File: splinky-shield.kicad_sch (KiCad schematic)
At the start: 40 parts, among them J1 USB_C_Receptacle_USB2.0, J2 Conn_01x12, J3 Conn_01x05, J4 Conn_01x12, J5 Conn_01x02, SW1 SW_Push, SW2 SW_Push, U1 RP2040, U2 GD25Q80CEIGR, U3 XC6210B332MR-G, Y1 Crystal_GND24

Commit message: routing
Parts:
- removed J2, J4: Conn_01x12, 0xLib_Connectors:PinHeader_1x12_P2.54mm, symbol Connector_Generic:Conn_01x12
- removed J3: Conn_01x05, 0xLib_Connectors:PinHeader_1x05_P2.54mm, symbol Connector_Generic:Conn_01x05
- added J10: Ribbon, Library:5_PinHeader, symbol Connector:Conn_01x05_Female
- added J11, J6: Serial, Library:Jack_3.5mm_PJ320E_Horizontal, symbol Connector:AudioJack4
- added J2, J3: Conn_01x04_Female, Connector_PinSocket_2.54mm:PinSocket_1x04_P2.54mm_Vertical, symbol Connector:Conn_01x04_Female
- added J7: trackball, Library:6_PinHeader, symbol Connector:Conn_01x06_Female
- added J8: Ribbon, Library:6_PinHeader, symbol Connector:Conn_01x06_Female
- added J9: RGB, Library:header1x03, symbol Connector:Conn_01x03_Female
- added JP1, JP2: Jumper_2_Open, local-libraries:SolderJumper-2_P1.3mm_Open_RoundedPad1.0x1.5mm, symbol Jumper:Jumper_2_Open
- added SW3: SW_SPST, Library:PushSwitch, symbol Switch:SW_SPST
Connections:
- net +5V: now also J2.1 (Pin_1), J3.1 (Pin_1), J7.1 (Pin_1), J9.1 (Pin_1), JP1.2 (B), JP2.2 (B)
- net D+: now also J2.4 (Pin_4), J3.4 (Pin_4)
- net D-: now also J2.3 (Pin_3), J3.3 (Pin_3)
- net GND: now also J11.R1, J2.2 (Pin_2), J3.2 (Pin_2), J6.R1, J7.6 (Pin_6), J9.2 (Pin_2), SW3.2 (B)
- net A0 renamed row2_l
- net row2_l: now also J10.5 (Pin_5)
- net A1 renamed col1_l
- net col1_l: now also J10.4 (Pin_4)
- net A2 renamed col2_l
- net col2_l: now also J10.3 (Pin_3)
- net A3 renamed row1_l
- net row1_l: now also J10.2 (Pin_2)
- net D0 renamed rgb_r
- net rgb_r: now also J9.3 (Pin_3)
- net D1 renamed serial_l
- net serial_l: now also J11.R2, J6.R2
- net D12: no longer names the net of U1.15 (GPIO12)
- net D13: no longer names the net of U1.16 (GPIO13)
- net D14: no longer names the net of U1.17 (GPIO14)
- net D15 renamed split_hand_l
- net D16 renamed ss_l
- net ss_l: now also J7.2 (Pin_2)
- net D2: no longer names the net of U1.4 (GPIO2)
- net D21 renamed col3_l
- net col3_l: now also J10.1 (Pin_1)
- net D3: no longer names the net of U1.5 (GPIO3)
- net D4 renamed row4_l
- net row4_l: now also J8.1 (Pin_1)
- net D5 renamed row3_l
- net row3_l: now also J8.2 (Pin_2)
- net D6 renamed col4_l
- net col4_l: now also J8.3 (Pin_3)
- net D7 renamed col5_l
- net col5_l: now also J8.4 (Pin_4)
- net D8 renamed col6_l
- net col6_l: now also J8.5 (Pin_5)
- net D9 renamed row5_l
- net row5_l: now also J8.6 (Pin_6)
- net MISO renamed miso_l
- net miso_l: now also J7.5 (Pin_5)
- net MOSI renamed mosi_l
- net mosi_l: now also J7.3 (Pin_3)
- net SCLK renamed sc_l
- net sc_l: now also J7.4 (Pin_4)
- net ~{RESET} renamed Rst
- net Rst: now also SW3.1 (A)
- new net: J6.T, JP1.1 (A)
- new net: J11.T, JP2.1 (A)
- no-connect marks 9 -> 16

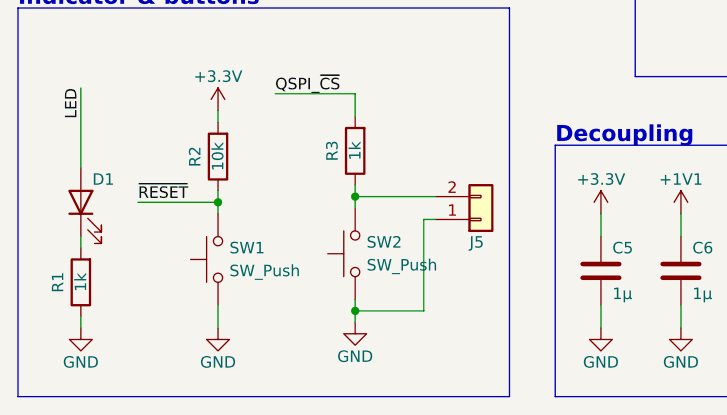
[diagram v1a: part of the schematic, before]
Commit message: remove buttons
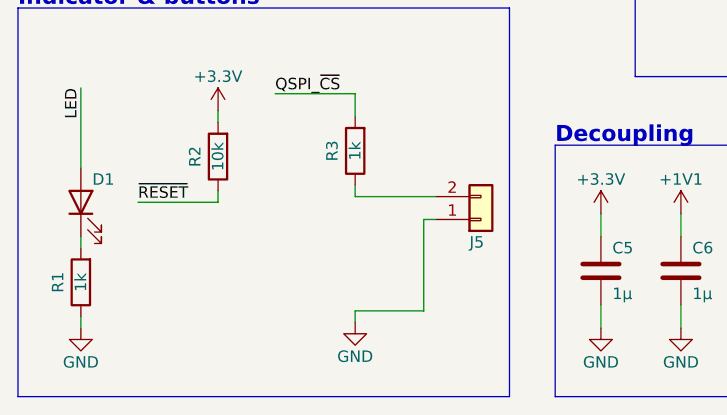
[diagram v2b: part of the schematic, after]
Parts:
- removed SW1, SW2: SW_Push, Button_Switch_SMD:SW_SPST_CK_KXT3, symbol Switch:SW_Push
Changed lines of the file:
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@@
   (junction (at 160.02 38.1) (diameter 0) (color 0 0 0 0)
   )
-  (junction (at 40.005 172.72) (diameter 0) (color 0 0 0 0)
-  )
   (junction (at 33.02 113.03) (diameter 0) (color 0 0 0 0)
   )
@@
   (junction (at 71.12 44.45) (diameter 0) (color 0 0 0 0)
   )
-  (junction (at 55.245 172.085) (diameter 0) (color 0 0 0 0)
-  )
   (junction (at 130.81 185.42) (diameter 0) (color 0 0 0 0)
   )
   (junction (at 97.79 106.68) (diameter 0) (color 0 0 0 0)
   )
-  (junction (at 55.245 184.785) (diameter 0) (color 0 0 0 0)
-  )
   (junction (at 33.02 115.57) (diameter 0) (color 0 0 0 0)
   )
@@
     (stroke (width 0) (type default) (color 0 0 0 0))
   )
-  (wire (pts (xy 40.005 184.15) (xy 40.005 186.69))
-    (stroke (width 0) (type default) (color 0 0 0 0))
-  )
   (wire (pts (xy 101.6 175.26) (xy 110.49 175.26))
     (stroke (width 0) (type default) (color 0 0 0 0))
@@
     (stroke (width 0) (type default) (color 0 0 0 0))
   )
-  (wire (pts (xy 55.245 172.085) (xy 55.245 173.355))
-    (stroke (width 0) (type default) (color 0 0 0 0))
-  )
   (wire (pts (xy 105.41 90.17) (xy 93.98 90.17))
     (stroke (width 0) (type default) (color 0 0 0 0))
@@
     (stroke (width 0) (type default) (color 0 0 0 0))
   )
-  (wire (pts (xy 55.245 183.515) (xy 55.245 184.785))
-    (stroke (width 0) (type default) (color 0 0 0 0))
-  )
   (wire (pts (xy 111.76 83.82) (xy 116.84 83.82))
     (stroke (width 0) (type default) (color 0 0 0 0))
@@
     (stroke (width 0) (type default) (color 0 0 0 0))
   )
-  (wire (pts (xy 40.005 172.72) (xy 40.005 173.99))
-    (stroke (width 0) (type default) (color 0 0 0 0))
-  )
   (wire (pts (xy 101.6 184.15) (xy 101.6 185.42))
     (stroke (width 0) (type default) (color 0 0 0 0))
@@
     (pin "1")
   )
-  (symbol (lib_id "Switch:SW_Push") (at 55.245 178.435 90) (unit 1)
-    (in_bom yes) (on_board yes) (fields_autoplaced)
-    (property "Reference" "SW2" (id 0) (at 56.515 177.1649 90)
-      (effects (font (size 1.27 1.27)) (justify right))
-    )
-    (property "Value" "SW_Push" (id 1) (at 56.515 179.7049 90)
-      (effects (font (size 1.27 1.27)) (justify right))
-    )
-    (property "Footprint" "Button_Switch_SMD:SW_SPST_CK_KXT3" (id 2) (at 50.165 178.435 0)
-      (effects (font (size 1.27 1.27)) hide)
-    )
-    (property "Datasheet" "~" (id 3) (at 50.165 178.435 0)
-      (effects (font (size 1.27 1.27)) hide)
-    )
-    (property "LCSC" "C319433" (id 4) (at 55.245 178.435 0)
-      (effects (font (size 1.27 1.27)) hide)
-    )
-    (pin "1")
-    (pin "2")
-  )
-  (symbol (lib_id "power:GND") (at 40.005 186.69 0) (unit 1)
-    (in_bom yes) (on_board yes)
-    (property "Reference" "#PWR05" (id 0) (at 40.005 193.04 0)
-      (effects (font (size 1.27 1.27)) hide)
-    )
-    (property "Value" "GND" (id 1) (at 40.005 190.5 0))
-    (property "Footprint" "" (id 2) (at 40.005 186.69 0)
-      (effects (font (size 1.27 1.27)) hide)
-    )
-    (property "Datasheet" "" (id 3) (at 40.005 186.69 0)
-      (effects (font (size 1.27 1.27)) hide)
-    )
-    (pin "1")
-  )
   (symbol (lib_id "Device:R") (at 198.12 111.125 180) (unit 1)
     (in_bom yes) (on_board yes)
@@
     (pin "2")
   )
-  (symbol (lib_id "Switch:SW_Push") (at 40.005 179.07 90) (unit 1)
-    (in_bom yes) (on_board yes) (fields_autoplaced)
-    (property "Reference" "SW1" (id 0) (at 41.275 177.7999 90)
-      (effects (font (size 1.27 1.27)) (justify right))
-    )
-    (property "Value" "SW_Push" (id 1) (at 41.275 180.3399 90)
-      (effects (font (size 1.27 1.27)) (justify right))
-    )
-    (property "Footprint" "Button_Switch_SMD:SW_SPST_CK_KXT3" (id 2) (at 34.925 179.07 0)
-      (effects (font (size 1.27 1.27)) hide)
-    )
-    (property "Datasheet" "~" (id 3) (at 34.925 179.07 0)
-      (effects (font (size 1.27 1.27)) hide)
-    )
-    (property "LCSC" "C319433" (id 4) (at 40.005 179.07 0)
-      (effects (font (size 1.27 1.27)) hide)
-    )
-    (pin "1")
-    (pin "2")
-  )
   (symbol (lib_id "power:+5V") (at 340.995 86.995 0) (unit 1)
     (in_bom yes) (on_board yes) (fields_autoplaced)
@@
       (reference "#PWR04") (unit 1) (value "+3.3V") (footprint "")
     )
-    (path "/4f8a166b-9702-4d80-b4fa-22089550ab5e"
-      (reference "#PWR05") (unit 1) (value "GND") (footprint "")
-    )
     (path "/d17eab26-feb4-4974-b911-181dda768f7a"
       (reference "#PWR06") (unit 1) (value "GND") (footprint "")
@@
       (reference "R11") (unit 1) (value "10k") (footprint "Resistor_SMD:R_0402_1005Metric")
     )
-    (path "/c30a3276-ac5c-4a68-880e-26478e1b53e4"
-      (reference "SW1") (unit 1) (value "SW_Push") (footprint "Button_Switch_SMD:SW_SPST_CK_KXT3")
-    )
-    (path "/4ea9bd29-a5a9-4d62-b350-c59ad41d14d5"
-      (reference "SW2") (unit 1) (value "SW_Push") (footprint "Button_Switch_SMD:SW_SPST_CK_KXT3")
-    )
     (path "/6d39e0e8-fc13-499e-b901-bbfc80821db7"

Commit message: routing
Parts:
- added J12, J4: Conn_01x04_Female, Connector_PinSocket_2.54mm:PinSocket_1x04_P2.54mm_Vertical, symbol Connector:Conn_01x04_Female
- added SW1: SW_SPST, Library:PushSwitch, symbol Switch:SW_SPST
- added U4: USBLC6-2P6, Package_TO_SOT_SMD:SOT-666, symbol Power_Protection:USBLC6-2P6
- J11, J6: footprint Library:Jack_3.5mm_PJ320E_Horizontal -> drawings:Jack_3.5mm_PJ320E_Horizontal_custom
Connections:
- net +5V: no longer J2.1 (Pin_1), J3.1 (Pin_1)
- net D+: now also J12.4 (Pin_4), J4.4 (Pin_4); no longer J1.A6 (D+), J1.B6 (D+), J2.4 (Pin_4), J3.4 (Pin_4)
- net D-: now also J12.3 (Pin_3), J4.3 (Pin_3); no longer J1.A7 (D-), J1.B7 (D-), J2.3 (Pin_3), J3.3 (Pin_3)
- net GND: now also J12.2 (Pin_2), J4.2 (Pin_2), SW1.2 (B); no longer FB1.1, J1.A1 (GND), J1.A12 (GND), J1.B1 (GND), J1.B12 (GND), J2.2 (Pin_2), J3.2 (Pin_2), R4.2, R5.2
- net Rst: now also SW1.1 (A)
- net VBUS: now also J12.1 (Pin_1), J4.1 (Pin_1); no longer J1.A4 (VBUS), J1.A9 (VBUS), J1.B4 (VBUS), J1.B9 (VBUS)
- new net D+_daughter: J1.A6 (D+), J1.B6 (D+), J2.4 (Pin_4), J3.4 (Pin_4), U4.3 (I/O2), U4.4 (I/O2)
- new net D-_daughter: J1.A7 (D-), J1.B7 (D-), J2.3 (Pin_3), J3.3 (Pin_3), U4.1 (I/O1), U4.6 (I/O1)
- new net Gnd_daughter: FB1.1, J1.A1 (GND), J1.A12 (GND), J1.B1 (GND), J1.B12 (GND), J2.2 (Pin_2), J3.2 (Pin_2), R4.2, R5.2, U4.2 (GND)
- new net Vbus_daughter: J1.A4 (VBUS), J1.A9 (VBUS), J1.B4 (VBUS), J1.B9 (VBUS), J2.1 (Pin_1), J3.1 (Pin_1), U4.5 (VBUS)
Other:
- note added: "ESD protection"
- note added: "Headers"
- moved on the sheet: FB1, J1, J2, J3, R4, R5

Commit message: silkscreen
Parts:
- removed SW1, SW3: SW_SPST, Library:PushSwitch, symbol Switch:SW_SPST
- added J13: Conn_01x02_Female, drawings:PinHeader_1x02_P1.27mm_Vertical, symbol Connector:Conn_01x02_Female
- J1: footprint 0xLib_USB_Type-C:USB_C_Receptacle_HRO_TYPE-C-31-M-14 -> drawings:GT-USB-7014C
- J12, J2, J3, J4: footprint Connector_PinSocket_2.54mm:PinSocket_1x04_P2.54mm_Vertical -> drawings:PinHeader_1x04_P2.54mm_Vertical
- J5: footprint Connector_PinHeader_1.27mm:PinHeader_1x02_P1.27mm_Vertical -> drawings:PinHeader_1x02_P1.27mm_Vertical
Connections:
- net GND: now also J13.2 (Pin_2)
- net Rst renamed ~{RESET}
- net ~{RESET}: now also J13.1 (Pin_1)

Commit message: license stuff
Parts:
- added SW1, SW2: SW_SPST, Library:PushSwitch, symbol Switch:SW_SPST
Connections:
- net GND: now also SW1.2 (B), SW2.2 (B)
- net ~{RESET}: now also SW1.1 (A), SW2.1 (A)
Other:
- company: plut0nium -> bastardkb
- title: 0xB2 - Splinky -> Splinky-shield
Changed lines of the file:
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@@
   (paper "A4")
   (title_block
-    (title "0xB2 - Splinky")
+    (title "Splinky-shield")
     (rev "2")
-    (company "plut0nium")
+    (company "bastardkb")
   )
   (junction (at 46.99 127) (diameter 0) (color 0 0 0 0)
@@
     (effects (font (size 1.27 1.27)) (justify left bottom))
   )
+  (label "~{RESET}" (at 44.45 205.105 180)
+    (effects (font (size 1.27 1.27)) (justify right bottom))
+  )
   (label "QSPI_~{CS}" (at 111.76 59.69 0)
     (effects (font (size 1.27 1.27)) (justify left bottom))
@@
     (effects (font (size 1.27 1.27)) (justify right bottom))
   )
+  (label "~{RESET}" (at 43.815 214.63 180)
+    (effects (font (size 1.27 1.27)) (justify right bottom))
+  )
   (label "QSPI_D0" (at 111.76 63.5 0)
     (effects (font (size 1.27 1.27)) (justify left bottom))
@@
     (pin "1")
   )
+  (symbol (lib_id "Switch:SW_SPST") (at 48.895 214.63 0) (unit 1)
+    (in_bom yes) (on_board yes)
+    (property "Reference" "SW1" (id 0) (at 48.895 208.28 0))
+    (property "Value" "SW_SPST" (id 1) (at 48.895 210.82 0))
+    (property "Footprint" "Library:PushSwitch" (id 2) (at 48.895 214.63 0)
+      (effects (font (size 1.27 1.27)) hide)
+    )
+    (property "Datasheet" "~" (id 3) (at 48.895 214.63 0)
+      (effects (font (size 1.27 1.27)) hide)
+    )
+    (pin "1")
+    (pin "2")
+  )
   (symbol (lib_id "Device:R") (at 120.65 93.98 90) (unit 1)
     (in_bom yes) (on_board yes)
@@
     (pin "2")
   )
+  (symbol (lib_id "power:GND") (at 53.975 214.63 90) (unit 1)
+    (in_bom yes) (on_board yes)
+    (property "Reference" "#PWR03" (id 0) (at 60.325 214.63 0)
+      (effects (font (size 1.27 1.27)) hide)
+    )
+    (property "Value" "GND" (id 1) (at 60.9599 214.786 90)
+      (effects (font (size 1.27 1.27)) (justify left))
+    )
+    (property "Footprint" "" (id 2) (at 53.975 214.63 0)
+      (effects (font (size 1.27 1.27)) hide)
+    )
+    (property "Datasheet" "" (id 3) (at 53.975 214.63 0)
+      (effects (font (size 1.27 1.27)) hide)
+    )
+    (pin "1")
+  )
   (symbol (lib_id "Device:C") (at 157.48 180.34 0) (unit 1)
     (in_bom yes) (on_board yes)
@@
     (pin "1")
   )
+  (symbol (lib_id "Switch:SW_SPST") (at 49.53 205.105 0) (unit 1)
+    (in_bom yes) (on_board yes)
+    (property "Reference" "SW2" (id 0) (at 49.53 198.755 0))
+    (property "Value" "SW_SPST" (id 1) (at 49.53 201.295 0))
+    (property "Footprint" "Library:PushSwitch" (id 2) (at 49.53 205.105 0)
+      (effects (font (size 1.27 1.27)) hide)
+    )
+    (property "Datasheet" "~" (id 3) (at 49.53 205.105 0)
+      (effects (font (size 1.27 1.27)) hide)
+    )
+    (pin "1")
+    (pin "2")
+  )
   (symbol (lib_id "Connector:Conn_01x03_Female") (at 388.747 32.512 0) (unit 1)
     (in_bom yes) (on_board yes)
@@
     (pin "1")
   )
+  (symbol (lib_id "power:GND") (at 54.61 205.105 90) (unit 1)
+    (in_bom yes) (on_board yes)
+    (property "Reference" "#PWR05" (id 0) (at 60.96 205.105 0)
+      (effects (font (size 1.27 1.27)) hide)
+    )
+    (property "Value" "GND" (id 1) (at 61.5949 205.261 90)
+      (effects (font (size 1.27 1.27)) (justify left))
+    )
+    (property "Footprint" "" (id 2) (at 54.61 205.105 0)
+      (effects (font (size 1.27 1.27)) hide)
+    )
+    (property "Datasheet" "" (id 3) (at 54.61 205.105 0)
+      (effects (font (size 1.27 1.27)) hide)
+    )
+    (pin "1")
+  )
   (symbol (lib_id "Device:C") (at 139.7 180.34 0) (unit 1)
     (in_bom yes) (on_board yes)
@@
       (reference "#PWR02") (unit 1) (value "+5V") (footprint "")
     )
+    (path "/29f0470e-d9ab-4e03-a28e-1f861067b19f"
+      (reference "#PWR03") (unit 1) (value "GND") (footprint "")
+    )
     (path "/08bb14e3-6da7-460c-adff-2a8900dee170"
       (reference "#PWR04") (unit 1) (value "+3.3V") (footprint "")
     )
+    (path "/c6f64293-5e29-4afa-8644-d8f9ea3d34e8"
+      (reference "#PWR05") (unit 1) (value "GND") (footprint "")
+    )
     (path "/d17eab26-feb4-4974-b911-181dda768f7a"
       (reference "#PWR06") (unit 1) (value "GND") (footprint "")
@@
       (reference "R11") (unit 1) (value "10k") (footprint "Resistor_SMD:R_0402_1005Metric")
     )
+    (path "/1b4533a2-d5e4-4403-b2a7-a0feb02c55e1"
+      (reference "SW1") (unit 1) (value "SW_SPST") (footprint "Library:PushSwitch")
+    )
+    (path "/7131ee3d-de36-4b6f-a391-6695d97d81c2"
+      (reference "SW2") (unit 1) (value "SW_SPST") (footprint "Library:PushSwitch")
+    )
     (path "/073e7a20-6222-4c9d-9f89-871bf718b9fb"
